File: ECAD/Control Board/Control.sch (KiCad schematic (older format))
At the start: 17 parts

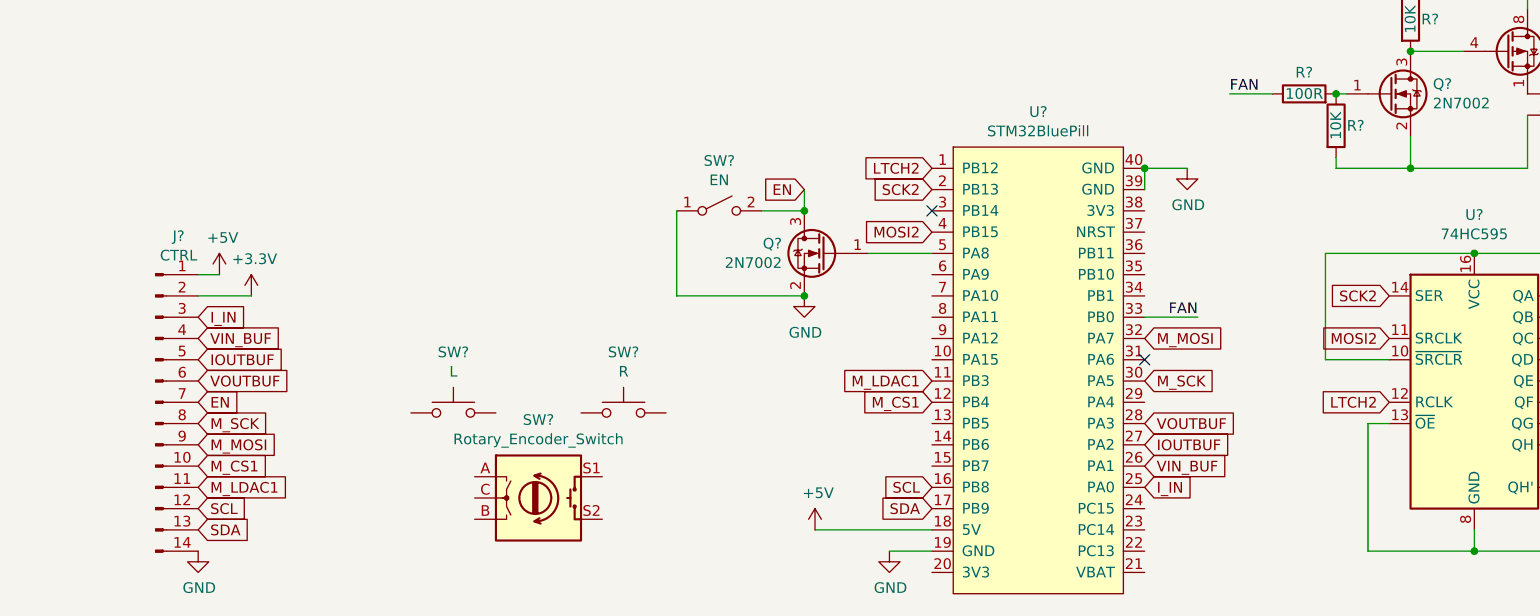
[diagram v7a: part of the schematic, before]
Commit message: cleanup main schematic, remove mppt circuitry
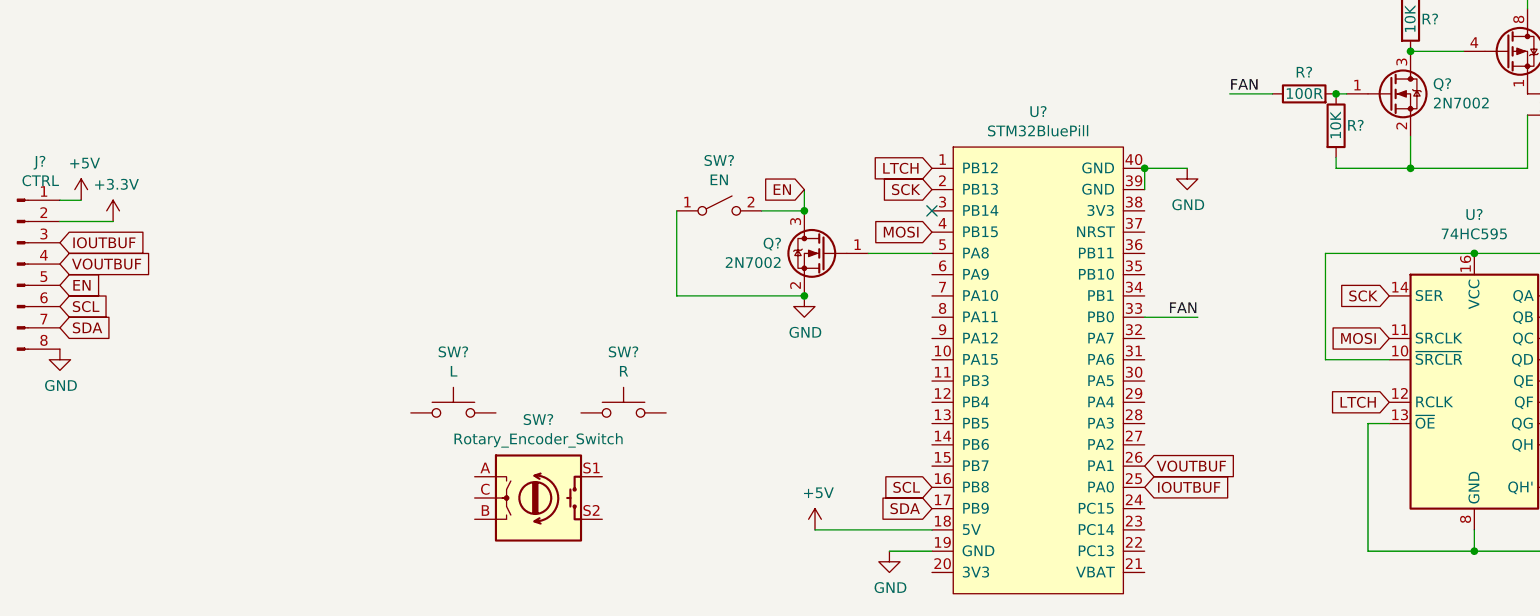
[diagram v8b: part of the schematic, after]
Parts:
- removed J?: CTRL, symbol Connector:Conn_01x14_Male
- added J?: CTRL, symbol Connector:Conn_01x08_Male
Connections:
- net I_IN is gone; now on net IOUTBUF: U?.25 (PA0)
- net VIN_BUF is gone; now on net VOUTBUF: U?.26 (PA1)
- net +3V3: now also J?.2 (Pin_2)
- net +5V: now also J?.1 (Pin_1)
- net EN: now also J?.5 (Pin_5)
- net GND: now also J?.8 (Pin_8)
- net IOUTBUF: now also J?.3 (Pin_3); no longer U?.27 (PA2)
- net SCL: now also J?.6 (Pin_6)
- net SDA: now also J?.7 (Pin_7)
- net VOUTBUF: now also J?.4 (Pin_4); no longer U?.28 (PA3)
- net LTCH2 renamed LTCH
- net MOSI2 renamed MOSI
- net M_CS1: no longer names the net of U?.12 (PB4)
- net M_LDAC1: no longer names the net of U?.11 (PB3)
- net M_MOSI: no longer names the net of U?.32 (PA7)
- net M_SCK: no longer names the net of U?.30 (PA5)
- net SCK2 renamed SCK
- no-connect marks 6 -> 5
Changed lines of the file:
@@
 $EndDescr
-$Comp
-L Connector:Conn_01x14_Male J?
-U 1 1 62052A04
-P 1650 3400
-F 0 "J?" H 1758 4181 50  0000 C CNN
-F 1 "CTRL" H 1758 4090 50  0000 C CNN
-F 2 "" H 1650 3400 50  0001 C CNN
-F 3 "~" H 1650 3400 50  0001 C CNN
-	1    1650 3400
-	1    0    0    -1
-$EndComp
 $Comp
 L power:+5V #PWR?
 U 1 1 62054280
-P 1950 2800
-F 0 "#PWR?" H 1950 2650 50  0001 C CNN
-F 1 "+5V" H 1965 2973 50  0000 C CNN
-F 2 "" H 1950 2800 50  0001 C CNN
-F 3 "" H 1950 2800 50  0001 C CNN
-	1    1950 2800
+P 1300 2450
+F 0 "#PWR?" H 1300 2300 50  0001 C CNN
+F 1 "+5V" H 1315 2623 50  0000 C CNN
+F 2 "" H 1300 2450 50  0001 C CNN
+F 3 "" H 1300 2450 50  0001 C CNN
+	1    1300 2450
 	1    0    0    -1
 $EndComp
@@
 L power:+3.3V #PWR?
 U 1 1 62054B41
-P 2100 2900
-F 0 "#PWR?" H 2100 2750 50  0001 C CNN
-F 1 "+3.3V" H 2115 3073 50  0000 C CNN
-F 2 "" H 2100 2900 50  0001 C CNN
-F 3 "" H 2100 2900 50  0001 C CNN
-	1    2100 2900
-	1    0    0    -1
-$EndComp
-Wire Wire Line
-	1950 2800 1850 2800
-Wire Wire Line
-	1850 2900 2100 2900
-Text GLabel 1850 3000 2    50   Input ~ 0
-I_IN
-Text GLabel 1850 3100 2    50   Input ~ 0
-VIN_BUF
-Text GLabel 1850 3200 2    50   Input ~ 0
+P 1450 2550
+F 0 "#PWR?" H 1450 2400 50  0001 C CNN
+F 1 "+3.3V" H 1465 2723 50  0000 C CNN
+F 2 "" H 1450 2550 50  0001 C CNN
+F 3 "" H 1450 2550 50  0001 C CNN
+	1    1450 2550
+	1    0    0    -1
+$EndComp
+Wire Wire Line
+	1300 2450 1200 2450
+Wire Wire Line
+	1200 2550 1450 2550
+Text GLabel 1200 2650 2    50   Input ~ 0
 IOUTBUF
-Text GLabel 1850 3300 2    50   Input ~ 0
+Text GLabel 1200 2750 2    50   Input ~ 0
 VOUTBUF
-Text GLabel 1850 3400 2    50   Input ~ 0
+Text GLabel 1200 2850 2    50   Input ~ 0
 EN
-Text GLabel 1850 3500 2    50   Input ~ 0
-M_SCK
-Text GLabel 1850 3600 2    50   Input ~ 0
-M_MOSI
-Text GLabel 1850 3700 2    50   Input ~ 0
-M_CS1
-Text GLabel 1850 3800 2    50   Input ~ 0
-M_LDAC1
 $Comp
 L power:GND #PWR?
 U 1 1 6205654B
-P 1850 4100
-F 0 "#PWR?" H 1850 3850 50  0001 C CNN
-F 1 "GND" H 1855 3927 50  0000 C CNN
-F 2 "" H 1850 4100 50  0001 C CNN
-F 3 "" H 1850 4100 50  0001 C CNN
-	1    1850 4100
+P 1200 3150
+F 0 "#PWR?" H 1200 2900 50  0001 C CNN
+F 1 "GND" H 1205 2977 50  0000 C CNN
+F 2 "" H 1200 3150 50  0001 C CNN
+F 3 "" H 1200 3150 50  0001 C CNN
+	1    1200 3150
 	1    0    0    -1
 $EndComp
@@
 Wire Wire Line
 	5100 4100 5300 4100
-Text GLabel 6300 3300 2    50   Input ~ 0
-M_SCK
-Text GLabel 6300 3100 2    50   Input ~ 0
-M_MOSI
 Text GLabel 4700 2400 0    50   Input ~ 0
 EN
@@
 	5000 2700 5300 2700
 Text GLabel 6300 3800 2    50   Input ~ 0
-I_IN
+IOUTBUF
 Text GLabel 6300 3700 2    50   Input ~ 0
-VIN_BUF
-Text GLabel 6300 3600 2    50   Input ~ 0
-IOUTBUF
-Text GLabel 6300 3500 2    50   Input ~ 0
 VOUTBUF
-Text GLabel 5300 3400 0    50   Input ~ 0
-M_CS1
-Text GLabel 5300 3300 0    50   Input ~ 0
-M_LDAC1
 $Comp
 L Switch:SW_SPST SW?
@@
 Connection ~ 9800 4100
 Text GLabel 5300 2600 0    50   Input ~ 0
-MOSI2
+MOSI
 Text GLabel 5300 2400 0    50   Input ~ 0
-SCK2
+SCK
 Text GLabel 5300 2300 0    50   Input ~ 0
-LTCH2
+LTCH
 Text GLabel 7450 3100 0    50   Input ~ 0
-MOSI2
+MOSI
 Text GLabel 7450 2900 0    50   Input ~ 0
-SCK2
+SCK
 Text GLabel 7450 3400 0    50   Input ~ 0
-LTCH2
+LTCH
 Wire Wire Line
 	7450 3500 7350 3500
@@
 	7150 2700 7850 2700
 Connection ~ 7850 2700
-NoConn ~ 6300 3200
 NoConn ~ 5300 2500
 $Comp
@@
 	1    0    0    -1
 $EndComp
-Text GLabel 1850 3900 2    50   Input ~ 0
+Text GLabel 1200 2950 2    50   Input ~ 0
 SCL
-Text GLabel 1850 4000 2    50   Input ~ 0
+Text GLabel 1200 3050 2    50   Input ~ 0
 SDA
 Text GLabel 5300 3800 0    50   Input ~ 0
@@
 Text GLabel 5300 3900 0    50   Input ~ 0
 SDA
+$Comp
+L Connector:Conn_01x08_Male J?
+U 1 1 6213E32B
+P 1000 2750
+F 0 "J?" H 1108 3231 50  0000 C CNN
+F 1 "CTRL" H 1108 3140 50  0000 C CNN
+F 2 "" H 1000 2750 50  0001 C CNN
+F 3 "~" H 1000 2750 50  0001 C CNN
+	1    1000 2750
+	1    0    0    -1
+$EndComp
 $EndSCHEMATC
